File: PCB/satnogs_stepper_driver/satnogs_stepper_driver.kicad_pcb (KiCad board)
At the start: 2 copper layers, 36.2 x 53.3 mm, 16 parts, among them P1 CONN_01X18, P2 CONN_01X02, P3 MOTOR 1, P4 MOTOR 2, U1 POLOLU_A4988, U2 POLOLU_A4988

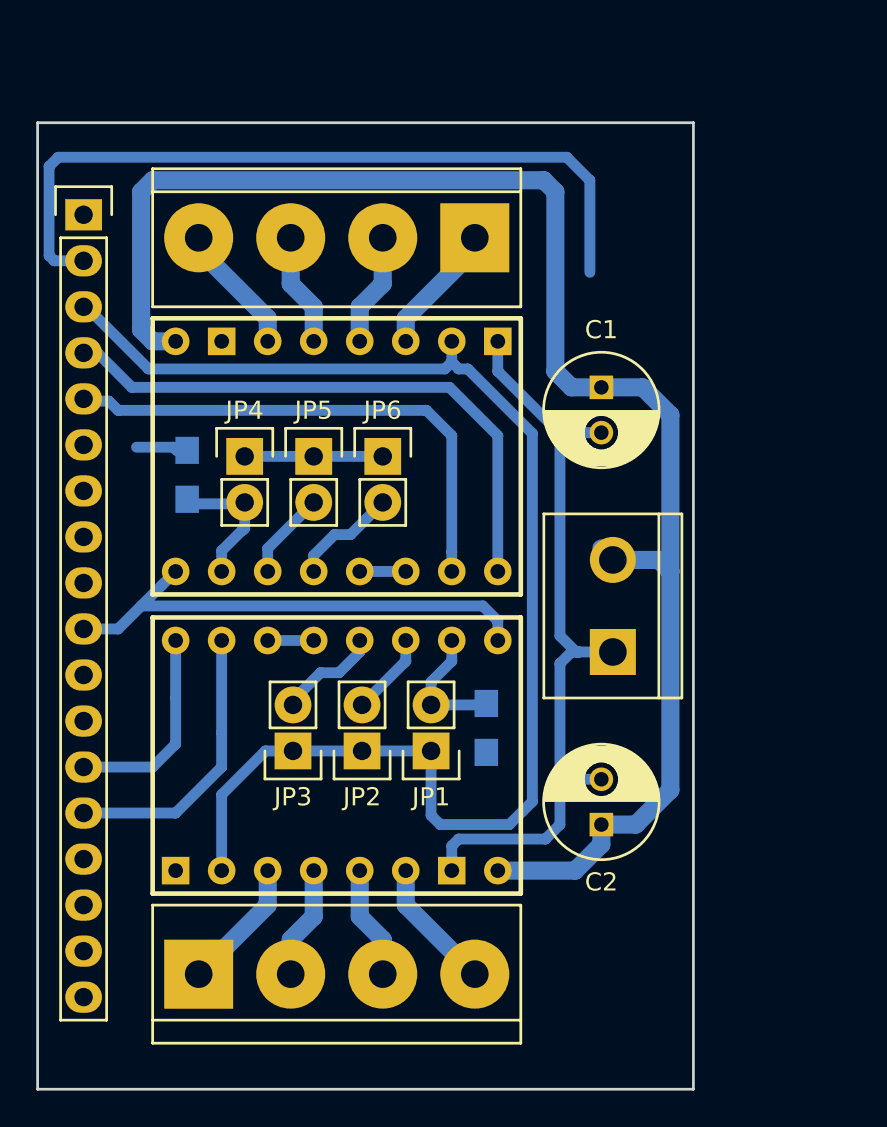
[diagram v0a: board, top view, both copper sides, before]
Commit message: Update stepper driver PCB, add BOM.
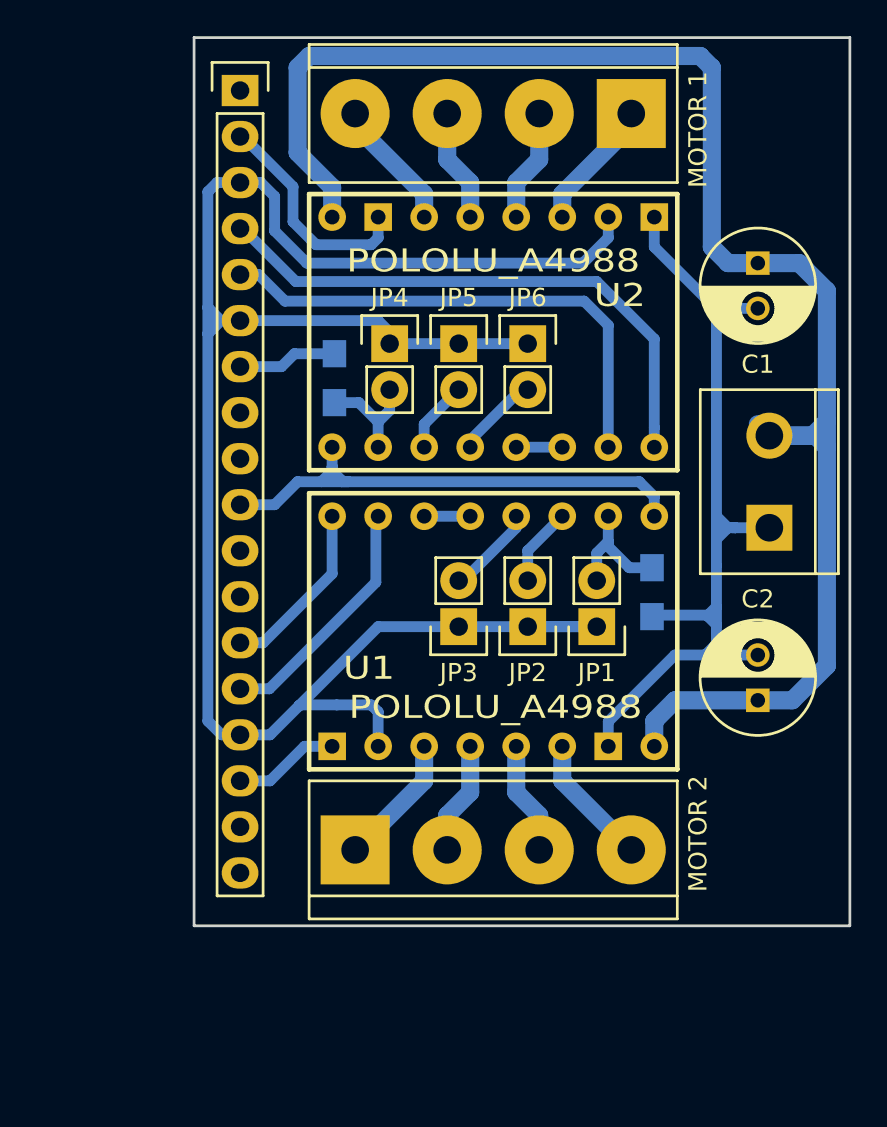
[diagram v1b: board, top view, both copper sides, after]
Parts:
- added ©2016 Libre Space Foundation : Stepper Driver, Symbols:Symbol_OSHW-Logo_SilkScreen, B.Cu at (166.4, 77.0)
- P1: value CONN_01X18 -> uC_Board
- P2: value CONN_01X02 -> POWER IN
- moved R1 11.8 mm to (159.0, 102.7)
- moved JP3 11.4 mm to (148.3, 104.6)
- moved JP1 11.4 mm to (156.0, 104.6)
- moved JP2 11.4 mm to (152.1, 104.6)
- moved P3 11.0 mm to (150.2, 76.3)
- moved P4 11.0 mm to (150.2, 117.0)
- moved U1 11.0 mm to (150.2, 104.9)
- moved U2 11.0 mm to (150.2, 88.4)
- moved C1 11.0 mm to (164.8, 84.6)
- moved C2 11.0 mm to (164.8, 108.7)
- moved P2 11.0 mm to (165.5, 96.6)
- moved P1 11.0 mm to (136.3, 75.1)
- moved JP4 10.1 mm to (144.5, 89.0)
- moved JP5 10.1 mm to (148.3, 89.0)
- moved JP6 10.1 mm to (152.1, 89.0)
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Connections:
- P1 pad 15: Net-(P1-Pad15) -> +5V
- P1 pad 16: Net-(P1-Pad16) -> GND
- P1 pad 6: Net-(P1-Pad6) -> +5V
- P1 pad 7: Net-(P1-Pad7) -> GND
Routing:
- net +5V: track 83.7 -> 110.6 mm
- net GND: track 89.1 -> 72.9 mm
- net /VMOT: track 87.5 -> 90.4 mm
- net /STEPM2: track 15.7 -> 13.9 mm
- net /DIRM2: track 11.3 -> 9.83 mm
- net /MS3M1: track 5.91 -> 4.71 mm
- net /MS1M1: track 7.57 -> 6.40 mm
- net /EN: track 27.5 -> 28.5 mm
- net /MS2M1: track 4.86 -> 3.96 mm
- net /DIRM1: track 32.2 -> 31.4 mm
- net /MS3M2: track 5.68 -> 5.02 mm
- added copper zone on B.Cu, net GND
- added copper zone on F.Cu, net GND
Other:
- board size 36.2 x 53.3 mm -> 36.2 x 49 mm
- board text added: "+5V"
- board text added: "DIR1"
- board text added: "DIR2"
- board text added: "EN"
- board text added: "GND"
- board text added: "STEP1"
- board text added: "STEP2"

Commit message: Small fixes.
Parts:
- moved P1 0.06 mm to (136.2, 75.1)
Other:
- board text added: "NC"
